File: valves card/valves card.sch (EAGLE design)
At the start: 68 parts, among them J1 09231486921, J2 TBP02R1-381-14BE, Q1 IRLZ44NSTRLPBF, Q11 IRLZ44NSTRLPBF, Q13 IRLZ44NSTRLPBF, Q15 IRLZ44NSTRLPBF, Q17 IRLZ44NSTRLPBF, Q19 IRLZ44NSTRLPBF, Q21 IRLZ44NSTRLPBF, Q23 IRLZ44NSTRLPBF, Q3 IRLZ44NSTRLPBF, Q5 IRLZ44NSTRLPBF, Q7 IRLZ44NSTRLPBF, Q9 IRLZ44NSTRLPBF, U1 LM2937IMP-10, U10 OR-815, U12 OR-815, U14 OR-815, U16 OR-815, U18 OR-815, U2 EL817(D)-ND, U20 OR-815, U22 OR-815, U24 OR-815, U4 OR-815, U6 OR-815, U8 OR-815

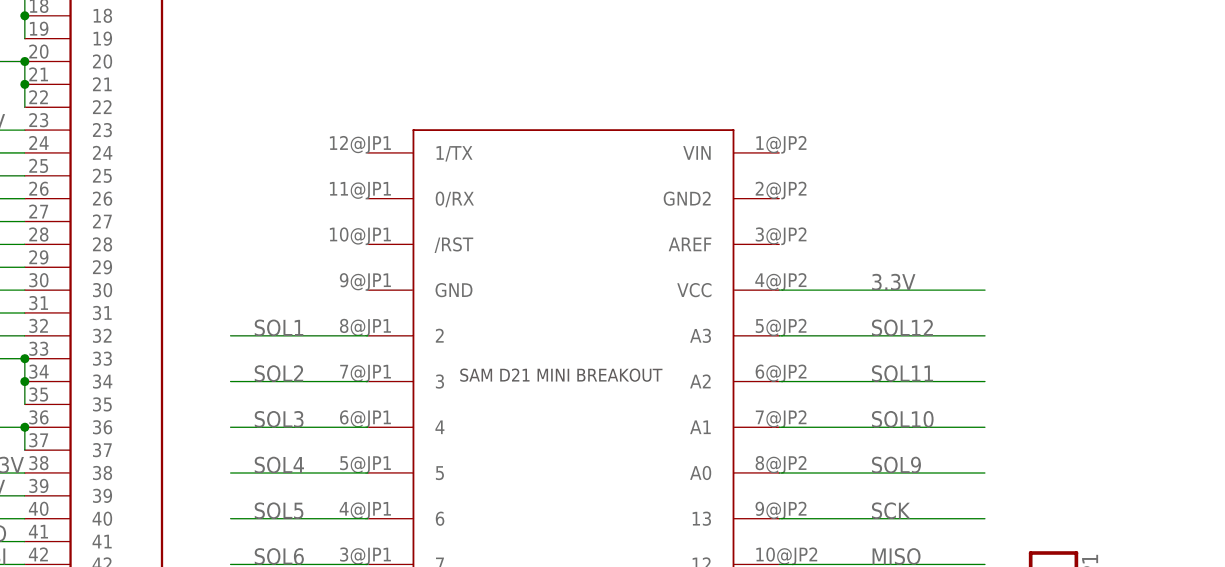
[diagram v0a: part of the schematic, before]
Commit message: re routed broken connections from last commit, parts should work now
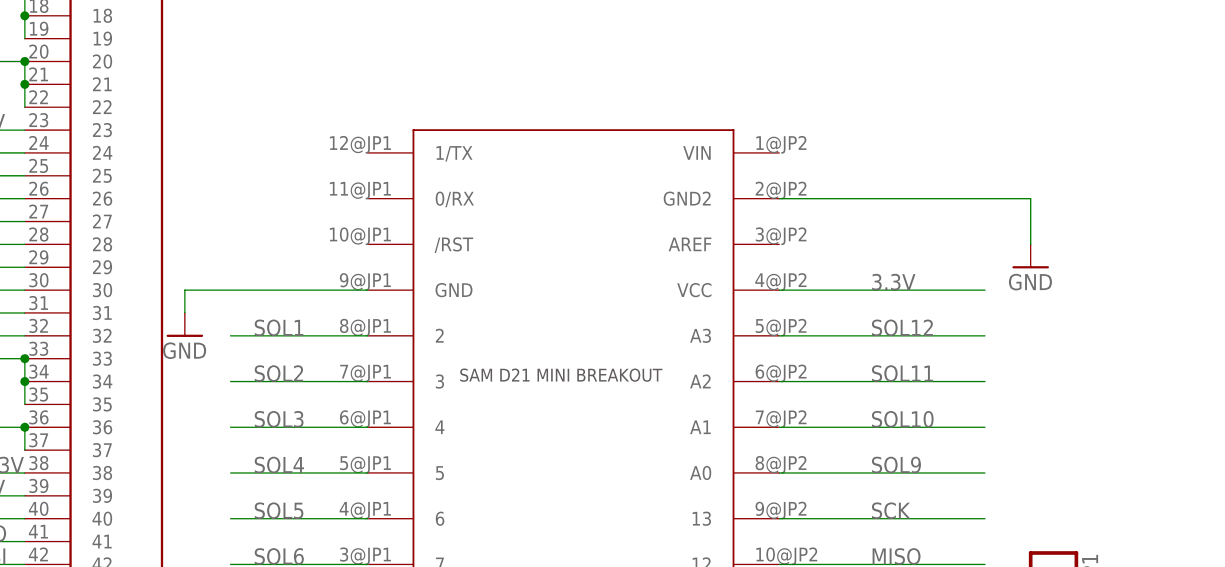
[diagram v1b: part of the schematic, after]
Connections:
- net GND: now also U$1.GND, U$1.GND2
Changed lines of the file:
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@@
 <part name="P1" library="pinhead" library_urn="urn:adsk.eagle:library:325" deviceset="PINHD-1X1" device="" package3d_urn="urn:adsk.eagle:package:22485/2"/>
 <part name="SJ1" library="SparkFun-Passives" deviceset="SOLDERJUMPER" device="TRACE"/>
+<part name="GND4" library="supply1" library_urn="urn:adsk.eagle:library:371" deviceset="GND" device=""/>
+<part name="GND5" library="supply1" library_urn="urn:adsk.eagle:library:371" deviceset="GND" device=""/>
 </parts>
 <sheets>
@@
 <attribute name="VALUE" x="124.46" y="7.62" size="1.778" layer="96"/>
 </instance>
+<instance part="GND4" gate="1" x="127" y="55.88" smashed="yes">
+<attribute name="VALUE" x="124.46" y="53.34" size="1.778" layer="96"/>
+</instance>
+<instance part="GND5" gate="1" x="33.02" y="48.26" smashed="yes">
+<attribute name="VALUE" x="30.48" y="45.72" size="1.778" layer="96"/>
+</instance>
 </instances>
 <busses>
@@
 <pinref part="R68" gate="G$1" pin="1"/>
 </segment>
+<segment>
+<pinref part="U$1" gate="G$1" pin="GND2"/>
+<wire x1="99.06" y1="63.5" x2="127" y2="63.5" width="0.1524" layer="91"/>
+<wire x1="127" y1="63.5" x2="127" y2="58.42" width="0.1524" layer="91"/>
+<pinref part="GND4" gate="1" pin="GND"/>
+</segment>
+<segment>
+<pinref part="U$1" gate="G$1" pin="GND"/>
+<wire x1="53.34" y1="53.34" x2="33.02" y2="53.34" width="0.1524" layer="91"/>
+<wire x1="33.02" y1="53.34" x2="33.02" y2="50.8" width="0.1524" layer="91"/>
+<pinref part="GND5" gate="1" pin="GND"/>
+</segment>
 </net>

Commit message: cleaned up valves board silkscreen, moved header forwards
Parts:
- removed Q1, Q11, Q13, Q15, Q17, Q19, Q21, Q23, Q3, Q5, Q7, Q9: IRLZ44NSTRLPBF, BUK9214-30A,118:BUK9214-30A-118-DPAK
- removed R37, R43, R49, R55, R61, R67: 600, eagle-ltspice:R
- removed R38, R44, R50, R56, R62, R68: 10k, eagle-ltspice:R
- removed R39, R45, R51, R57, R63, R69: 100, eagle-ltspice:R
- removed U14, U16, U18, U20, U22, U24: OR-815, EL817C:EL817C
- added R10, R12, R23, R28, R30, R5: 10k, eagle-ltspice:R
- added R11, R16, R22, R29, R34, R4: 600, eagle-ltspice:R
- added R17, R18, R24, R35, R36, R6: 100, eagle-ltspice:R
- added T1, T10, T11, T12, T2, T3, T4, T5, T6, T7, T8, T9: IRLZ44NSTRLPBF, BUK9214-30A,118:BUK9214-30A-118-DPAK
- added U11, U13, U3, U5, U7, U9: EL817(D)-ND, EL817C:EL817C
- C1: value 10Uf -> 0.1Uf; device eagle-ltspice:CC1206 -> eagle-ltspice:C
- C2: value 0.1Uf -> 10Uf; device eagle-ltspice:C -> eagle-ltspice:CC1206
- J1: value 09231486921 -> TBP02R1-381-14BE; device din41612_48_pin_board:09231486921 -> TBP02R1-381-14BE:TBP02R1-381-14BE
- J2: value TBP02R1-381-14BE -> 09231486921; device TBP02R1-381-14BE:TBP02R1-381-14BE -> din41612_48_pin_board:09231486921
- M1: value (none) -> SAM_D21_MINI_BREAKOUT
- R1, R19: value 600 -> 10k
- R2, R20: value 10k -> 600
- R21, R3: value 100 -> 10k
- R26, R8: value 10k -> 100
- U1: value LM2937IMP-10 -> LM2937IMP-12
- U10, U12, U6, U8: value OR-815 -> EL817(D)-ND
- U4: value OR-815 -> EL817(D)-ND; MP OR-815 -> (none)
- renumbered P1 to JP1, U$1 to M1
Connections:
- removed net N$23 (its old number): R15.2, U6.A
- removed net N$58 (its old number): R49.1, U18.E
- removed net N$59 (its old number): R51.2, U18.A
- removed net N$70 (its old number): R61.1, U22.E
- new net N$16: R4.1, U3.E
- new net N$17: R8.2, U3.A
- new net N$35: R17.2, U6.A
- new net N$40: R16.1, U7.E
- net 12V: now also C2.1, U11.C, U13.C, U3.C, U5.C, U7.C, U9.C; no longer C1.1, U14.C, U16.C, U18.C, U20.C, U22.C, U24.C
- net 24V: now also C1.1, J1.1, J1.2, J2.20, J2.21, J2.22, J2.36, J2.37, J2.5, J2.6; no longer C2.1, J1.20, J1.21, J1.22, J1.36, J1.37, J1.5, J1.6, J2.1, J2.2
- net 3.3V: now also J2.38; no longer J1.38
- net 5V: now also J2.23, J2.39; no longer J1.23, J1.39
- net DRAIN1: now also J1.14, T1.D; no longer J2.14, Q1.D
- net DRAIN10: now also J1.5, T10.D; no longer J2.5, Q19.D
- net DRAIN11: now also J1.4, T11.D; no longer J2.4, Q21.D
- net DRAIN12: now also J1.3, T12.D; no longer J2.3, Q23.D
- net DRAIN2: now also J1.13, T2.D; no longer J2.13, Q3.D
- net DRAIN3: now also J1.12, T3.D; no longer J2.12, Q5.D
- net DRAIN4: now also J1.11, T4.D; no longer J2.11, Q7.D
- net DRAIN5: now also J1.10, T5.D; no longer J2.10, Q9.D
- net DRAIN6: now also J1.9, T6.D; no longer J2.9, Q11.D
- net DRAIN7: now also J1.8, T7.D; no longer J2.8, Q13.D
- net DRAIN8: now also J1.7, T8.D; no longer J2.7, Q15.D
- net DRAIN9: now also J1.6, T9.D; no longer J2.6, Q17.D
- net EXT_1: now also J2.15; no longer J1.15
- net EXT_2: now also J2.16; no longer J1.16
- net EXT_3: now also J2.31; no longer J1.31
- net EXT_4: now also J2.32; no longer J1.32
- net EXT_5: now also J2.46; no longer J1.46
- net EXT_6: now also J2.47; no longer J1.47
- net EXT_7: now also J2.48; no longer J1.48
- net GND: now also J2.1, J2.17, J2.18, J2.19, J2.2, J2.3, J2.33, J2.34, J2.35, J2.4, R1.1, R10.1, R12.1, R19.1, R21.1, R23.1, R28.1, R3.1, R30.1, R5.1, T1.S, T10.S, T11.S, T12.S, T2.S, T3.S, T4.S, T5.S, T6.S, T7.S, T8.S, T9.S, U11.K, U13.K, U3.K, U5.K, U7.K, U9.K; no longer J1.1, J1.17, J1.18, J1.19, J1.2, J1.3, J1.33, J1.34, J1.35, J1.4, Q1.S, Q11.S, Q13.S, Q15.S, Q17.S, Q19.S, Q21.S, Q23.S, Q3.S, Q5.S, Q7.S, Q9.S, R2.1, R20.1, R26.1, R38.1, R44.1, R50.1, R56.1, R62.1, R68.1, R8.1, U14.K, U16.K, U18.K, U20.K, U22.K, U24.K
- net MISO: now also J2.41; no longer J1.41
- net MOSI: now also J2.42; no longer J1.42
- net N$10: now also T1.G; no longer Q1.G
- net N$11: now also R2.1; no longer R1.1
- net N$15: now also R3.2, R4.2, T2.G; no longer Q3.G, R7.2, R8.2
- net N$21: now also R5.2, R7.2, T3.G; no longer Q5.G, R13.2, R14.2
- net N$27: now also R10.2, R11.2, T4.G; no longer Q7.G, R19.2, R20.2
- net N$28: now also R11.1, U5.E; no longer R19.1, U8.E
- net N$29: now also R15.2, U5.A; no longer R21.2, U8.A
- net N$33: now also R12.2, R13.2, T5.G; no longer Q9.G, R25.2, R26.2
- net N$39: now also R14.2, R16.2, T6.G; no longer Q11.G, R31.2, R32.2
- net N$41: now also R18.2, U7.A; no longer R33.2, U12.A
- net N$45: now also R19.2, R20.2, T7.G; no longer Q13.G, R37.2, R38.2
- net N$46: now also R20.1, U8.E; no longer R37.1, U14.E
- net N$47: now also R24.2, U8.A; no longer R39.2, U14.A
- net N$5: now also R6.2; no longer R3.2
- net N$51: now also R21.2, R22.2, T8.G; no longer Q15.G, R43.2, R44.2
- net N$52: now also R22.1, U9.E; no longer R43.1, U16.E
- net N$53: now also R26.2, U9.A; no longer R45.2, U16.A
- net N$57: now also R23.2, R25.2, T9.G; no longer Q17.G, R49.2, R50.2
- net N$63: now also R28.2, R29.2, T10.G; no longer Q19.G, R55.2, R56.2
- net N$64: now also R29.1, U11.E; no longer R55.1, U20.E
- net N$65: now also R33.2, U11.A; no longer R57.2, U20.A
- net N$69: now also R30.2, R31.2, T11.G; no longer Q21.G, R61.2, R62.2
- net N$71: now also R35.2, U12.A; no longer R63.2, U22.A
- net N$75: now also R32.2, R34.2, T12.G; no longer Q23.G, R67.2, R68.2
- net N$76: now also R34.1, U13.E; no longer R67.1, U24.E
- net N$77: now also R36.2, U13.A; no longer R69.2, U24.A
- net SCK: now also J2.40; no longer J1.40
- net SCL: now also J2.44; no longer J1.44
- net SDA: now also J2.43; no longer J1.43
- net SOL1: now also R6.1; no longer R3.1
- net SOL10: now also R33.1; no longer R57.1
- net SOL11: now also R35.1; no longer R63.1
- net SOL12: now also R36.1; no longer R69.1
- net SOL2: now also R8.1; no longer R9.1
- net SOL3: now also R9.1; no longer R15.1
- net SOL4: now also R15.1; no longer R21.1
- net SOL5: now also R17.1; no longer R27.1
- net SOL6: now also R18.1; no longer R33.1
- net SOL7: now also R24.1; no longer R39.1
- net SOL8: now also R26.1; no longer R45.1
- net SOL9: now also R27.1; no longer R51.1
- net SS_1: now also J2.8; no longer J1.8
- net SS_10: now also J2.26; no longer J1.26
- net SS_11: now also J2.27; no longer J1.27
- net SS_12: now also J2.28; no longer J1.28
- net SS_13: now also J2.29; no longer J1.29
- net SS_14: now also J2.30; no longer J1.30
- net SS_15: now also J2.45; no longer J1.45
- net SS_2: now also J2.9; no longer J1.9
- net SS_3: now also J2.10; no longer J1.10
- net SS_4: now also J2.11; no longer J1.11
- net SS_5: now also J2.12; no longer J1.12
- net SS_6: now also J2.13; no longer J1.13
- net SS_7: now also J2.14; no longer J1.14
- net SS_8: now also J2.24; no longer J1.24
- net SS_9: now also J2.25; no longer J1.25
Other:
- moved on the sheet: C1, C2, R1, R13, R14, R15, R19, R2, R20, R21, R25, R26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
